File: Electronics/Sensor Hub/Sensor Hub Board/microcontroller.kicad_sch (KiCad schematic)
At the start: 51 parts, among them IC302 STM32H723ZGT6, IC303 TJA1057GT/3, J301 TC2030, J302 Screw_Terminal_01x03, J303 TYPE-C-31-M-12, SW301 SW_DIP_x02, U301 USBLC6-4SC6-ES, U302 USBLC6-4SC6-ES, X301 25MHz_Clock, X302 32.768kHz_Clock

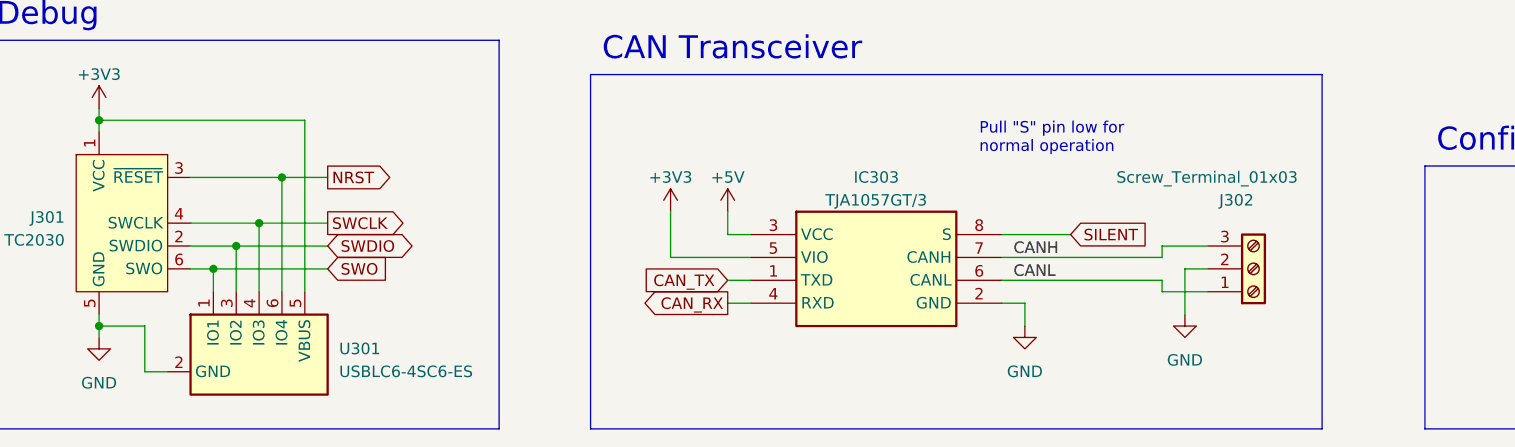
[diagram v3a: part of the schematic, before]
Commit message: Gateway board layout complete and routing begun
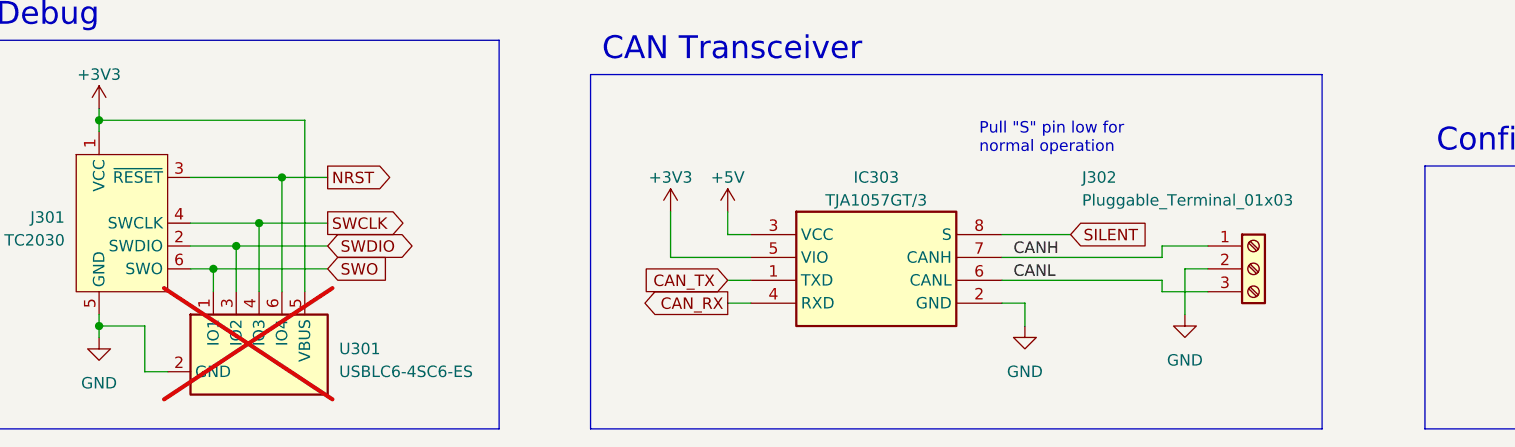
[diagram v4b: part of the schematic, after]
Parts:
- removed J302: Screw_Terminal_01x03, TerminalBlock:TerminalBlock_bornier-3_P5.08mm, symbol Connector:Screw_Terminal_01x03
- added J302: Pluggable_Terminal_01x03, MSL Footprints:Pluggable_terminal-3_P5.08mm, symbol MSL_Symbols:Pluggable_Terminal_01x03
- U301: now not fitted; now left out of the parts list
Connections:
- net CANH: now also J302.1 (Pin_1)
- net CANL: now also J302.3 (Pin_3)
- net GND: now also J302.2 (Pin_2)
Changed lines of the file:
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@@
+    )
+  )
+  (symbol (lib_id "MSL_Symbols:Pluggable_Terminal_01x03") (at 160.02 261.62 0) (unit 1)
+    (in_bom yes) (on_board yes) (dnp no)
+    (property "Reference" "J302" (at 140.97 251.46 0)
+      (effects (font (size 1.27 1.27)) (justify left))
+    )
+    (property "Value" "Pluggable_Terminal_01x03" (at 140.97 254 0)
+      (effects (font (size 1.27 1.27)) (justify left))
+    )
+    (property "Footprint" "MSL Footprints:Pluggable_terminal-3_P5.08mm" (at 160.02 261.62 0)
+      (effects (font (size 1.27 1.27)) hide)
+    )
+    (property "Datasheet" "~" (at 160.02 261.62 0)
+      (effects (font (size 1.27 1.27)) hide)
+    )
+    (pin "1")
+    (pin "2")
+    (pin "3")
+    (instances
+      (project "Sensor Hub Board"
+        (path "/5318664d-e328-4e84-a383-7318275dc447/86a04d6c-5487-4291-b767-6da69e96f7da"
+          (reference "J302") (unit 1)
+        )
+      )
     )
   )
@@
     )
   )
-  (symbol (lib_id "Connector:Screw_Terminal_01x03") (at 160.02 261.62 0) (mirror x) (unit 1)
-    (in_bom yes) (on_board yes) (dnp no)
-    (property "Reference" "J302" (at 156.21 254 0)
-      (effects (font (size 1.27 1.27)) (justify left))
-    )
-    (property "Value" "Screw_Terminal_01x03" (at 144.78 251.46 0)
-      (effects (font (size 1.27 1.27)) (justify left))
-    )
-    (property "Footprint" "TerminalBlock:TerminalBlock_bornier-3_P5.08mm" (at 160.02 261.62 0)
-      (effects (font (size 1.27 1.27)) hide)
-    )
-    (property "Datasheet" "~" (at 160.02 261.62 0)
-      (effects (font (size 1.27 1.27)) hide)
-    )
-    (pin "1")
-    (pin "2")
-    (pin "3")
-    (instances
-      (project "Sensor Hub Board"
-        (path "/5318664d-e328-4e84-a383-7318275dc447/86a04d6c-5487-4291-b767-6da69e96f7da"
-          (reference "J302") (unit 1)
-        )
-      )
-      (project "Power Board"
-        (path "/d8843e0a-fd8a-4193-ba57-f0164156e030/fab43204-4de8-48e9-a4c9-80bcd4a9c27a"
-          (reference "J303") (unit 1)
-        )
-      )
-    )
-  )
   (symbol (lib_id "power:+3V3") (at 181.61 82.55 0) (unit 1)
     (in_bom yes) (on_board yes) (dnp no) (fields_autoplaced)
@@
   )
   (symbol (lib_id "MSL_Symbols:USBLC6-4SC6-ES") (at 49.53 271.78 0) (unit 1)
-    (in_bom yes) (on_board yes) (dnp no) (fields_autoplaced)
+    (in_bom no) (on_board no) (dnp yes) (fields_autoplaced)
     (property "Reference" "U301" (at 58.42 270.51 0)
       (effects (font (size 1.27 1.27)) (justify left))

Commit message: Sensor hub board done
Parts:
- added C20: 10n, Capacitor_SMD:C_0402_1005Metric, symbol Device:C_Small
- added J417: JST_SH_1mm_1x4, MSL Footprints:JST_SH_1mm_1x4, symbol MSL_Symbols:JST_SH_1mm_1x4
- added R23: 10k, Resistor_SMD:R_0402_1005Metric, symbol Device:R_Small
- added R6 (x2): 2k2, Resistor_SMD:R_0402_1005Metric, symbol Device:R_Small
- added S302: TS20-42-25-WT-160-SMT-TR, MSL Footprints:TS204225WT160SMTTRMSL, symbol TS20-42-25-WT-160-SMT-TR-MSL:TS20-42-25-WT-160-SMT-TR
- J301: footprint Connector:Tag-Connect_TC2030-IDC-FP_2x03_P1.27mm_Vertical -> MSL Footprints:Tag-Connect_TC2030-IDC-FP_2x03_P1.27mm_Vertical; symbol Connector:Conn_ARM_SWD_TagConnect_TC2030 -> MSL_Symbols:TC2030
- renumbered IC303 to IC301
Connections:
- net +3V3: now also J417.2, R23.2, R6.1, R6.1
- net BTN: now also IC302.90 (PG5), C20.1, R23.1, S302.2 (NO_2)
- net CC1: now also U302.3 (IO2); no longer U302.1 (IO1)
- net CC2: now also U302.1 (IO1); no longer U302.3 (IO2)
- net GND: now also C20.2, J417.1, S302.3 (COM_1)
- net GPIO0A: now also IC302.40 (PA4)
- net GPIO0B: now also IC302.36 (PA2)
- net GPIO10A: now also IC302.142 (PE1)
- net GPIO10B: now also IC302.135 (PB5)
- net GPIO11A: now also IC302.134 (PB4)
- net GPIO11B: now also IC302.141 (PE0)
- net GPIO12A: now also IC302.119 (PD5)
- net GPIO12B: now also IC302.118 (PD4)
- net GPIO13A: now also IC302.117 (PD3)
- net GPIO13B: now also IC302.116 (PD2)
- net GPIO14A: now also IC302.113 (PC12)
- net GPIO14B: now also IC302.112 (PC11)
- net GPIO15A: now also IC302.111 (PC10)
- net GPIO15B: now also IC302.110 (PA15)
- net GPIO1A: now also IC302.37 (PA3)
- net GPIO1B: now also IC302.41 (PA5)
- net GPIO2A: now also IC302.66 (PE13)
- net GPIO2B: now also IC302.67 (PE14)
- net GPIO3A: now also IC302.42 (PA6)
- net GPIO3B: now also IC302.43 (PA7)
- net GPIO4A: now also IC302.64 (PE11)
- net GPIO5A: now also IC302.69 (PB10)
- net GPIO5B: now also IC302.70 (PB11)
- net GPIO6A: now also IC302.49 (PF11)
- net GPIO6B: now also IC302.48 (PB2)
- net GPIO7A: now also IC302.47 (PB1)
- net GPIO7B: now also IC302.46 (PB0)
- net GPIO8A: now also IC302.12 (PF2)
- net GPIO8B: now also IC302.11 (PF1)
- net GPIO9A: now also IC302.10 (PF0)
- net GPIO9B: now also IC302.7 (PC13)
- net IMU_CS: now also IC302.18 (PF6); no longer IC302.40 (PA4)
- net IMU_INT1: now also IC302.2 (PE3)
- net IMU_INT2: now also IC302.26 (PC0)
- net IMU_MISO: now also IC302.20 (PF8); no longer IC302.42 (PA6)
- net IMU_MOSI: now also IC302.21 (PF9); no longer IC302.43 (PA7)
- net IMU_SCK: now also IC302.19 (PF7); no longer IC302.41 (PA5)
- net LEDB: now also IC302.75 (PB14)
- net LEDG: now also IC302.73 (PB12)
- net LEDR: now also IC302.74 (PB13)
- net MAG_CS: now also IC302.3 (PE4); no longer IC302.73 (PB12)
- net MAG_DRDY: now also IC302.27 (PC1)
- net MAG_INT: now also IC302.28 (PC2_C)
- net MAG_MISO: now also IC302.4 (PE5); no longer IC302.75 (PB14)
- net MAG_MOSI: now also IC302.5 (PE6); no longer IC302.76 (PB15)
- net MAG_SCK: now also IC302.1 (PE2); no longer IC302.74 (PB13)
- net MUX1_RST: now also IC302.139 (PB8)
- net MUX2_RST: now also IC302.44 (PC4)
- net SILENT: now also IC302.34 (PA0)
- net USB_DN: now also U302.4 (IO3); no longer U302.6 (IO4)
- net USB_DP: now also U302.6 (IO4); no longer U302.4 (IO3)
- net VREF+: no longer C307.1, C309.1, FB1.1, IC302.33 (VDDA)
- net SCL3_MCU: now reaches IC302.100 (PA8)
- net SCL3_MCU: now also R6.2, J417.4
- net SCL4_MCU: now reaches IC302.54 (PF14)
- net SCL4_MCU: now also R6.2
- net SDA4_MCU: now reaches IC302.55 (PF15)
- net SDA4_MCU: now also R6.2
- net GPIO4B: now reaches IC302.65 (PE12)
- net SDA3_MCU: now reaches IC302.99 (PC9)
- net SDA3_MCU: now also R6.2, J417.3
- removed net SCL2_MCU: IC302.11 (PF1), R6.2
- removed net SDA2_MCU: IC302.10 (PF0), R6.2
- new net VDDA: C307.1, C309.1, FB1.1, IC302.33 (VDDA)
- now unconnected: J303.S1 (SHIELD), J303.S2 (SHIELD), J303.S3 (SHIELD), J303.S4 (SHIELD)
- no-connect marks 9 -> 61
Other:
- note added: "User Button"
- moved on the sheet: C304, C305, C307, C309, R6

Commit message: All boards done
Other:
- moved on the sheet: J417
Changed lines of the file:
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@@
   (no_connect (at 36.83 210.82))
   (no_connect (at 245.11 143.51))
-  (no_connect (at 281.94 240.03))
+  (no_connect (at 354.33 59.69))
   (no_connect (at 245.11 133.35))
   (no_connect (at 245.11 176.53))
@@
   (no_connect (at 245.11 181.61))
   (no_connect (at 374.65 149.86))
-  (no_connect (at 281.94 242.57))
+  (no_connect (at 354.33 62.23))
   (no_connect (at 204.47 212.09))
   (no_connect (at 245.11 153.67))
@@
     (stroke (width 0) (type default))
   )
-  (wire (pts (xy 276.86 234.95) (xy 281.94 234.95))
+  (wire (pts (xy 349.25 54.61) (xy 354.33 54.61))
     (stroke (width 0) (type default))
   )
@@
     (stroke (width 0) (type default))
   )
-  (wire (pts (xy 279.4 227.33) (xy 279.4 237.49))
+  (wire (pts (xy 351.79 46.99) (xy 351.79 57.15))
     (stroke (width 0) (type default))
   )
@@
     (stroke (width 0) (type default))
   )
-  (wire (pts (xy 276.86 224.79) (xy 276.86 229.87))
+  (wire (pts (xy 349.25 44.45) (xy 349.25 49.53))
     (stroke (width 0) (type default))
   )
@@
     (stroke (width 0) (type default))
   )
-  (wire (pts (xy 281.94 227.33) (xy 279.4 227.33))
+  (wire (pts (xy 354.33 46.99) (xy 351.79 46.99))
     (stroke (width 0) (type default))
   )
@@
     (stroke (width 0) (type default))
   )
-  (wire (pts (xy 276.86 229.87) (xy 281.94 229.87))
+  (wire (pts (xy 349.25 49.53) (xy 354.33 49.53))
     (stroke (width 0) (type default))
   )
@@
     (stroke (width 0) (type default))
   )
-  (wire (pts (xy 276.86 232.41) (xy 281.94 232.41))
+  (wire (pts (xy 349.25 52.07) (xy 354.33 52.07))
     (stroke (width 0) (type default))
   )
@@
     )
   )
-  (global_label "SCL3_MCU" (shape input) (at 276.86 234.95 180) (fields_autoplaced)
+  (global_label "SCL3_MCU" (shape input) (at 349.25 54.61 180) (fields_autoplaced)
     (effects (font (size 1.27 1.27)) (justify right))
-    (property "Intersheetrefs" "${INTERSHEET_REFS}" (at 264.2176 234.95 0)
+    (property "Intersheetrefs" "${INTERSHEET_REFS}" (at 336.6076 54.61 0)
       (effects (font (size 1.27 1.27)) (justify right) hide)
     )
@@
     )
   )
-  (global_label "SDA3_MCU" (shape bidirectional) (at 276.86 232.41 180) (fields_autoplaced)
+  (global_label "SDA3_MCU" (shape bidirectional) (at 349.25 52.07 180) (fields_autoplaced)
     (effects (font (size 1.27 1.27)) (justify right))
-    (property "Intersheetrefs" "${INTERSHEET_REFS}" (at 263.0458 232.41 0)
+    (property "Intersheetrefs" "${INTERSHEET_REFS}" (at 335.4358 52.07 0)
       (effects (font (size 1.27 1.27)) (justify right) hide)
     )
@@
     )
   )
-  (symbol (lib_id "power:GND") (at 279.4 237.49 0) (unit 1)
+  (symbol (lib_id "power:GND") (at 351.79 57.15 0) (unit 1)
     (in_bom yes) (on_board yes) (dnp no) (fields_autoplaced)
-    (property "Reference" "#PWR0441" (at 279.4 243.84 0)
+    (property "Reference" "#PWR0441" (at 351.79 63.5 0)
       (effects (font (size 1.27 1.27)) hide)
     )
-    (property "Value" "GND" (at 279.4 242.57 0)
+    (property "Value" "GND" (at 351.79 62.23 0)
       (effects (font (size 1.27 1.27)))
     )
-    (property "Footprint" "" (at 279.4 237.49 0)
+    (property "Footprint" "" (at 351.79 57.15 0)
       (effects (font (size 1.27 1.27)) hide)
     )
-    (property "Datasheet" "" (at 279.4 237.49 0)
+    (property "Datasheet" "" (at 351.79 57.15 0)
       (effects (font (size 1.27 1.27)) hide)
     )
@@
     )
   )
-  (symbol (lib_id "power:+3V3") (at 276.86 224.79 0) (unit 1)
+  (symbol (lib_id "power:+3V3") (at 349.25 44.45 0) (unit 1)
     (in_bom yes) (on_board yes) (dnp no) (fields_autoplaced)
-    (property "Reference" "#PWR0442" (at 276.86 228.6 0)
+    (property "Reference" "#PWR0442" (at 349.25 48.26 0)
       (effects (font (size 1.27 1.27)) hide)
     )
-    (property "Value" "+3V3" (at 276.86 220.98 0)
+    (property "Value" "+3V3" (at 349.25 40.64 0)
       (effects (font (size 1.27 1.27)))
     )
-    (property "Footprint" "" (at 276.86 224.79 0)
+    (property "Footprint" "" (at 349.25 44.45 0)
       (effects (font (size 1.27 1.27)) hide)
     )
-    (property "Datasheet" "" (at 276.86 224.79 0)
+    (property "Datasheet" "" (at 349.25 44.45 0)
       (effects (font (size 1.27 1.27)) hide)
     )
@@
     )
   )
-  (symbol (lib_id "MSL_Symbols:JST_SH_1mm_1x4") (at 289.56 232.41 0) (unit 1)
+  (symbol (lib_id "MSL_Symbols:JST_SH_1mm_1x4") (at 361.95 52.07 0) (unit 1)
     (in_bom yes) (on_board yes) (dnp no)
-    (property "Reference" "J417" (at 289.56 219.71 0)
+    (property "Reference" "J417" (at 361.95 39.37 0)
       (effects (font (size 1.27 1.27)))
     )
-    (property "Value" "JST_SH_1mm_1x4" (at 289.56 222.25 0)
+    (property "Value" "JST_SH_1mm_1x4" (at 361.95 41.91 0)
       (effects (font (size 1.27 1.27)))
     )
-    (property "Footprint" "MSL Footprints:JST_SH_1mm_1x4" (at 289.56 232.41 0)
+    (property "Footprint" "MSL Footprints:JST_SH_1mm_1x4" (at 361.95 52.07 0)
       (effects (font (size 1.27 1.27)) (justify bottom) hide)
     )
-    (property "Datasheet" "" (at 289.56 232.41 0)
+    (property "Datasheet" "" (at 361.95 52.07 0)
       (effects (font (size 1.27 1.27)) hide)
     )
-    (property "MANUFACTURER" "JST" (at 289.56 232.41 0)
+    (property "MANUFACTURER" "JST" (at 361.95 52.07 0)
       (effects (font (size 1.27 1.27)) (justify bottom) hide)
     )
-    (property "STANDARD" "Manufacturer recommendations" (at 289.56 232.41 0)
+    (property "STANDARD" "Manufacturer recommendations" (at 361.95 52.07 0)
       (effects (font (size 1.27 1.27)) (justify bottom) hide)
     )
